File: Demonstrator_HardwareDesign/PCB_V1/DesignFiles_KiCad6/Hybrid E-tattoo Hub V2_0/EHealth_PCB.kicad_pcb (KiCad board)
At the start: 2 copper layers, 50 x 50 mm, 55 parts, among them J1 Conn_01x06, J2 Conn_01x06, J3 Conn_01x06, J4 Conn_01x06, J4-OffTheShelf-Digital1 Conn_02x06_Counter_Clockwise, T1 BSC320N20NS3_G, U1 TCA9548APWR, U2 DEBO DCDC DOWN 4

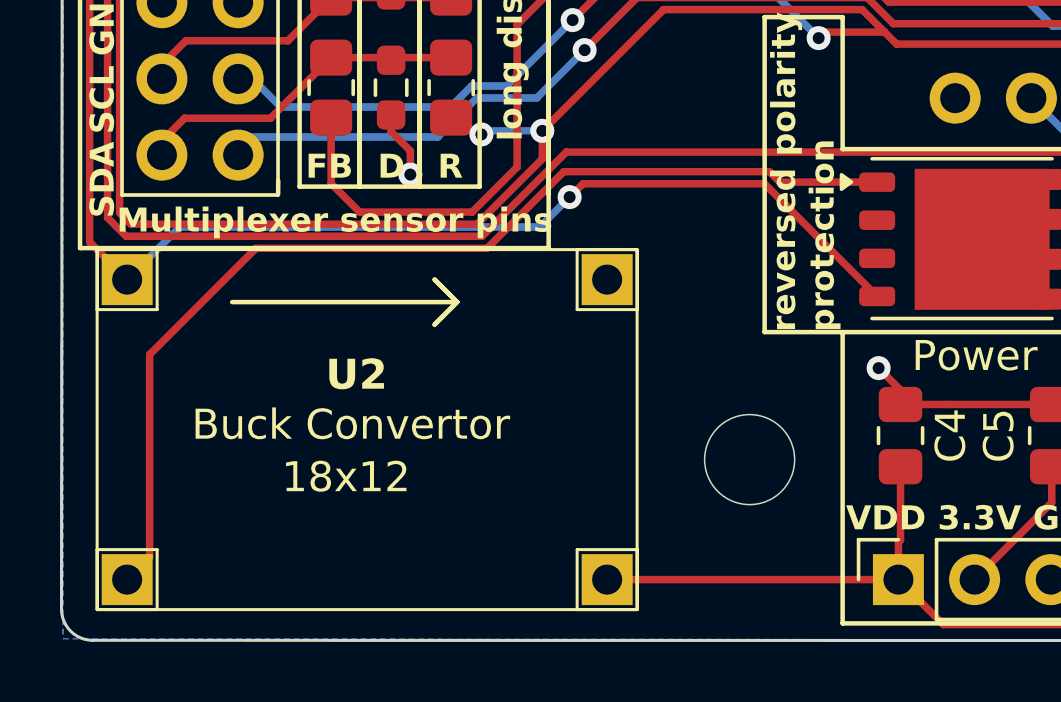
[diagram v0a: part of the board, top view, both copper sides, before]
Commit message: Added production files for V2.0
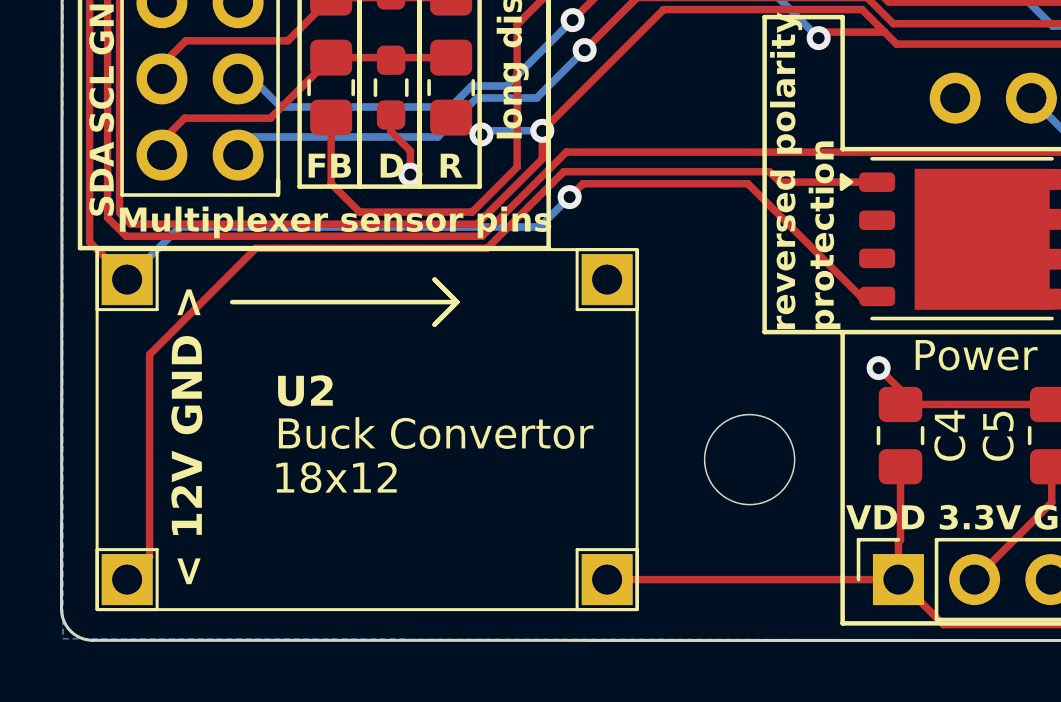
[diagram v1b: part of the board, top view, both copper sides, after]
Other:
- board text added: "< 12V GND >"
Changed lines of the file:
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@@
 		(at 188.75 97.25)
 		(property "Reference" "U2"
-			(at -0.353829 0.17519 0)
+			(at -2.06 0.7432 0)
 			(unlocked yes)
 			(layer "F.SilkS")
@@
 	)
 	(gr_text "Buck Convertor"
-		(at 182.896171 99.67519 0)
+		(at 185.674 99.9998 0)
 		(layer "F.SilkS")
 		(effects
@@
 		)
 	)
+	(gr_text "< 12V GND >"
+		(at 183.3626 104.5464 90)
+		(layer "F.SilkS")
+		(effects
+			(font
+				(size 1 1)
+				(thickness 0.2)
+				(bold yes)
+			)
+			(justify left bottom)
+		)
+	)
 	(gr_text "TX"
 		(at 191.2 69.2 0)
@@
 	)
 	(gr_text "18x12"
-		(at 185.896171 101.42519 0)
+		(at 185.5724 101.473 0)
 		(layer "F.SilkS")
 		(effects
@@
 	)
 	(segment
-		(start 195.5 91.5)
-		(end 195.9452 91.0548)
-		(width 0.25)
-		(layer "F.Cu")
-		(net 22)
-	)
-	(segment
 		(start 185.17 58.79)
 		(end 183.63 57.25)
@@
 	)
 	(segment
-		(start 201.992987 91.0548)
-		(end 205.75 94.811813)
+		(start 195.5 91.5)
+		(end 195.9452 91.0548)
+		(width 0.25)
+		(layer "F.Cu")
+		(net 22)
+	)
+	(segment
+		(start 195.9452 91.0548)
+		(end 201.4432 91.0548)
+		(width 0.25)
+		(layer "F.Cu")
+		(net 22)
+	)
+	(segment
+		(start 201.4432 91.0548)
+		(end 205.200213 94.811813)
 		(width 0.25)
 		(layer "F.Cu")
@@
 	)
 	(segment
-		(start 195.9452 91.0548)
-		(end 201.992987 91.0548)
+		(start 205.200213 94.811813)
+		(end 205.75 94.811813)
 		(width 0.25)
 		(layer "F.Cu")
